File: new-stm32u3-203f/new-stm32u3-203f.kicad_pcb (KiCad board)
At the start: 4 copper layers, 14.5 x 90 mm, 81 parts, among them J1 Display, J2 SJ-3524-SMT, J3 12401826E412A, J4 Battery connector, J5 473092651, J6 UART, J7 RESET, SW1 SW_SPDT, SW3 VOL+, SW4 VOL-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

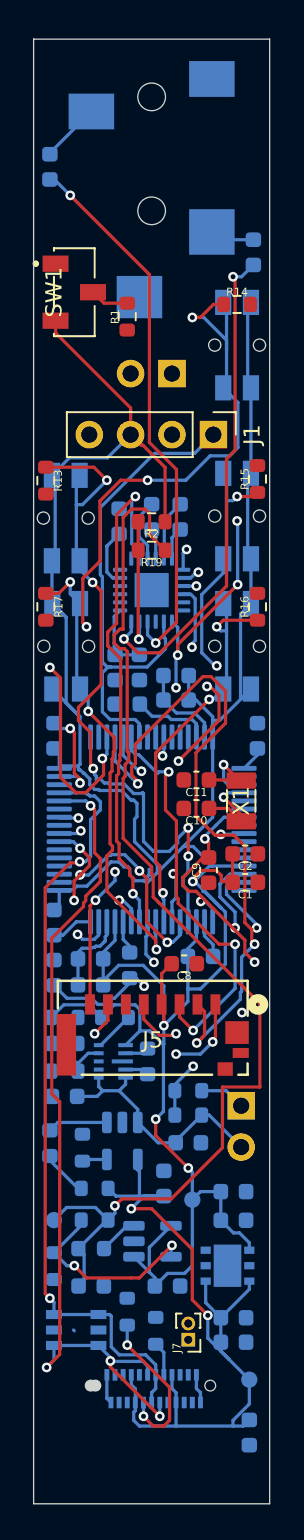
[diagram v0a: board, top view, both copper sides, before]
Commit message: restarted routing and started using 6 layers and power planes.
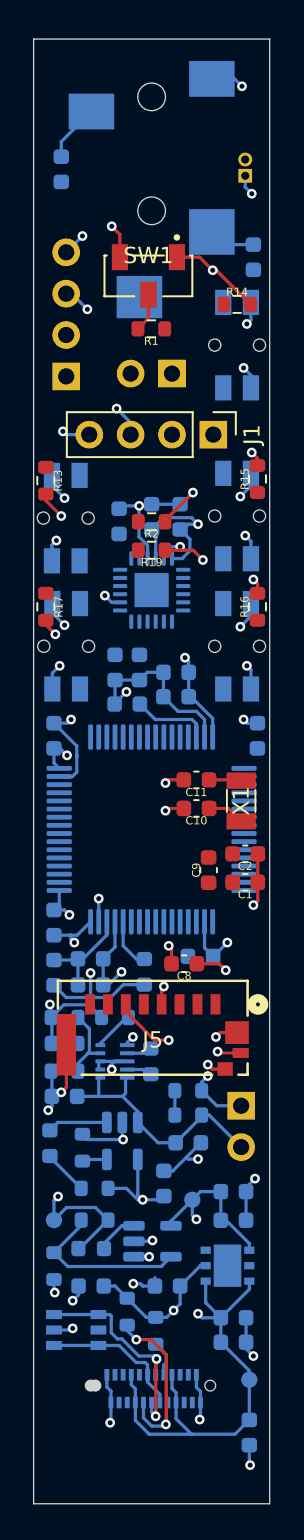
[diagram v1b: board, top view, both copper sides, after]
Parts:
- added J8: SWD, Connector_PinHeader_2.54mm:PinHeader_1x04_P2.54mm_Vertical, B.Cu at (149.0, 81.1)
- J7: moved to B.Cu
- moved J7 71.6 mm to (160.0, 68.8), turned to 0 degrees
- moved SW1 4.66 mm to (154.1, 75.0), turned to 180 degrees
- moved R1 1.66 mm to (154.2, 78.2), turned to 180 degrees
- moved L1 0.98 mm to (153.8, 117.7)
- moved C12 0.72 mm to (148.7, 68.4), turned to 90 degrees
- moved C13 0.30 mm to (160.5, 73.8), turned to 90 degrees
- moved C21 0.20 mm to (155.8, 100.8)
- moved C23 0.20 mm to (155.8, 99.3)
- moved L3 0.20 mm to (154.2, 123.2)
- moved U7 0.10 mm to (152.0, 123.2)
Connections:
- C1 pad 1: GNDA -> USB_GND
- C10 pad 2: GNDA -> USB_GND
- C11 pad 2: GNDA -> USB_GND
- C14 pad 2: GNDA -> USB_GND
- C15 pad 1: GNDA -> USB_GND
- C16 pad 1: GNDA -> USB_GND
- C17 pad 1: GNDA -> USB_GND
- C18 pad 1: GNDA -> USB_GND
- C19 pad 2: GNDA -> USB_GND
- C2 pad 1: GNDA -> USB_GND
- C21 pad 1: GNDA -> USB_GND
- C22 pad 1: GNDA -> USB_GND
- C23 pad 1: GNDA -> USB_GND
- C24 pad 1: GNDA -> USB_GND
- C25 pad 1: GNDA -> USB_GND
- C26 pad 1: GNDA -> USB_GND
- C27 pad 1: GNDA -> USB_GND
- C28 pad 1: GNDA -> USB_GND
- C29 pad 1: GNDA -> USB_GND
- C3 pad 2: GNDA -> USB_GND
- C30 pad 1: GNDA -> USB_GND
- C31 pad 1: GNDA -> USB_GND
- C33 pad 1: GNDA -> USB_GND
- C34 pad 1: GNDA -> USB_GND
- C35 pad 1: GNDA -> USB_GND
- C36 pad 1: GNDA -> USB_GND
- C4 pad 2: GNDA -> USB_GND
- C5 pad 1: GNDA -> USB_GND
- C6 pad 1: GNDA -> USB_GND
- C7 pad 1: GNDA -> USB_GND
- C8 pad 1: GNDA -> USB_GND
- C9 pad 1: GNDA -> USB_GND
- CR1 pad 2: GNDA -> USB_GND
- J1 pad 4: GNDA -> USB_GND
- J2 pad R: (no net) -> HP_RIGHT
- J2 pad S: (no net) -> USB_GND
- J2 pad T: (no net) -> HP_LEFT
- J4 pad 1: GNDA -> USB_GND
- J5 pad 6: GNDA -> USB_GND
- J5 pad G1: GNDA -> USB_GND
- J5 pad G2: GNDA -> USB_GND
- J5 pad G3: GNDA -> USB_GND
- J5 pad G4: GNDA -> USB_GND
- J7 pad 1: GNDA -> USB_GND
- R10 pad 2: GNDA -> USB_GND
- R13 pad 2: GNDA -> USB_GND
- R14 pad 2: GNDA -> USB_GND
- R15 pad 2: GNDA -> USB_GND
- R16 pad 2: GNDA -> USB_GND
- R17 pad 2: GNDA -> USB_GND
- R18 pad 2: GNDA -> USB_GND
- R4 pad 1: GNDA -> USB_GND
- R5 pad 2: GNDA -> USB_GND
- R7 pad 2: GNDA -> USB_GND
- R9 pad 1: GNDA -> USB_GND
- SW1 pad 1: GNDA -> USB_GND
- U1 pad 12: GNDA -> USB_GND
- U1 pad 18: GNDA -> USB_GND
- U1 pad 30: GNDA -> USB_GND
- U1 pad 32: GNDA -> USB_GND
- U1 pad 46: unconnected-(U1A-PA13-Pad46) -> SWDCLK
- U1 pad 47: GNDA -> USB_GND
- U1 pad 49: unconnected-(U1A-PA14-Pad49) -> SWDDIO
- U1 pad 63: GNDA -> USB_GND
- U2 pad 14: GNDA -> USB_GND
- U2 pad 21: GNDA -> USB_GND
- U2 pad 23: GNDA -> USB_GND
- U4 pad 2: GNDA -> USB_GND
- U4 pad 7: GNDA -> USB_GND
- U5 pad 2: GNDA -> USB_GND
- U6 pad 2: GNDA -> USB_GND
- U7 pad 2: GNDA -> USB_GND
- U7 pad 3: GNDA -> USB_GND
- U7 pad 8: GNDA -> USB_GND
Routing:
- net AVDD: track 197.0 -> 62.0 mm, vias 4 -> 25
- net USB_GND: track 3.61 -> 121.5 mm, vias 0 -> 42
- net sk_btn_2: track 61.2 -> 0.00 mm, vias 6 -> 0
- net UART_TX: track 53.2 -> 0.00 mm, vias 1 -> 0
- net +1V8: track 72.2 -> 21.0 mm, vias 1 -> 4
- net SD_DAT2: track 47.6 -> 0.00 mm, vias 4 -> 0
- net UART_RX: track 45.5 -> 0.00 mm, vias 1 -> 0
- net USB_D-: track 52.5 -> 8.87 mm, vias 4 -> 0
- net ps_btn_1: track 43.1 -> 0.00 mm, vias 5 -> 0
- net SD_DAT3: track 42.5 -> 0.00 mm, vias 3 -> 0
- net /MCU_IO/NRST: track 37.5 -> 0.00 mm, vias 3 -> 0
- net UBS_D+: track 47.4 -> 13.7 mm
- net v+_btn_3: track 33.1 -> 0.00 mm, vias 5 -> 0
- net DAC_RST: track 32.0 -> 0.00 mm, vias 2 -> 0
- net GNDA: track 31.9 -> 0.00 mm, vias 2 -> 0
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- added copper zone on In2.Cu, net +1V8
- added copper zone on In3.Cu, net AVDD
- added copper zone on In1.Cu, net USB_GND
- added copper zone on In4.Cu, net USB_GND
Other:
- copper layers 4 -> 6

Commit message: finished routing, need angus to check
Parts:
- moved J7 76.5 mm to (148.2, 144.4)
- moved C11 6.14 mm to (160.4, 100.8), turned to 90 degrees
- moved C10 3.33 mm to (160.3, 108.1), turned to -90 degrees
- moved X1 2.64 mm to (160.2, 104.6)
- moved C22 2.03 mm to (159.2, 116.2), turned to -90 degrees
- moved C9 0.65 mm to (157.1, 111.5)
- turned C12 to -90 degrees
- turned C13 to -90 degrees
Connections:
- J2 pad R: HP_RIGHT -> Net-(J2-R)
- J2 pad T: HP_LEFT -> Net-(J2-L)
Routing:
- net sk_btn_2: track 0.00 -> 56.3 mm, vias 0 -> 5
- net +1V8: track 21.0 -> 77.3 mm, vias 4 -> 3
- net v+_btn_3: track 0.00 -> 55.9 mm, vias 0 -> 3
- net ps_btn_1: track 0.00 -> 50.8 mm, vias 0 -> 3
- net /MCU_IO/NRST: track 0.00 -> 47.1 mm, vias 0 -> 1
- net UART_TX: track 0.00 -> 40.0 mm, vias 0 -> 1
- net pp_btn_5: track 0.00 -> 39.4 mm, vias 0 -> 4
- net UART_RX: track 0.00 -> 38.5 mm, vias 0 -> 1
- net USB_D-: track 8.87 -> 47.0 mm, vias 0 -> 2
- net UBS_D+: track 13.7 -> 49.1 mm, vias 2 -> 4
- net HP_RIGHT: track 3.54 -> 38.2 mm, vias 0 -> 2
- net I2C_SDA: track 0.00 -> 34.1 mm, vias 0 -> 2
- net DAC_RST: track 0.00 -> 31.4 mm, vias 0 -> 2
- net I2C1_SCL: track 0.00 -> 30.4 mm
- net HP_LEFT: track 2.87 -> 33.1 mm, vias 0 -> 2
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- added copper zone on B.Cu, net USB_GND
- added copper zone on F.Cu, net USB_GND
- added copper zone on In2.Cu, net USB_GND
- removed copper zone on In2.Cu, net +1V8

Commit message: ficxed all the vias and some routing, will need to add in ground stitching
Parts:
- moved C11 1.41 mm to (159.4, 101.8), turned to 0 degrees
- moved R2 0.95 mm to (154.2, 89.1)
- moved C25 0.45 mm to (160.3, 103.2)
- moved C18 0.30 mm to (156.3, 89.8)
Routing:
- net AVDD: track 74.7 -> 93.1 mm, vias 28 -> 25
- net USB_GND: track 132.8 -> 135.9 mm, vias 53 -> 49
- net +1V8: track 77.3 -> 74.7 mm
- net OSC_IN: track 6.98 -> 9.37 mm
- net OSC_OUT: track 5.48 -> 6.76 mm
- net Net-(U2-LDOIN/HPVDD): track 8.20 -> 9.17 mm
- net SCK_A: track 27.8 -> 28.6 mm
- net SWDCLK: track 27.8 -> 28.4 mm

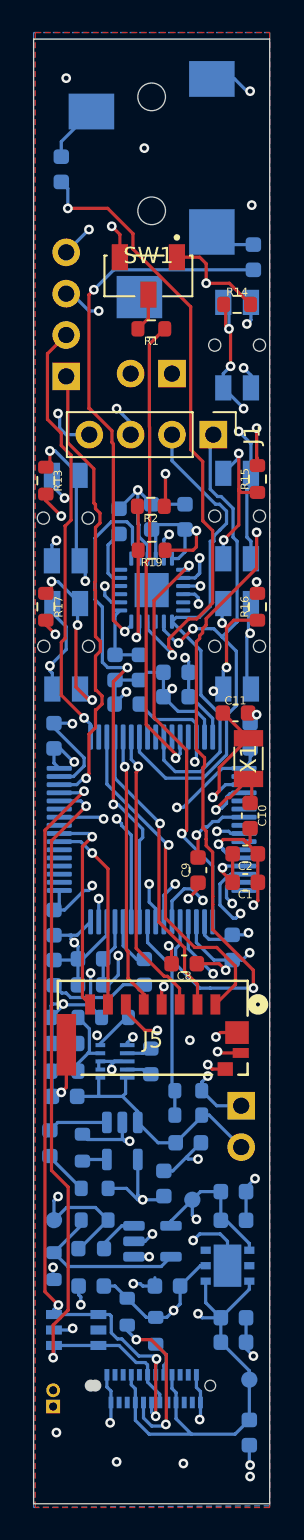
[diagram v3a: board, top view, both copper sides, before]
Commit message: added usb sheilding and more stiching vias
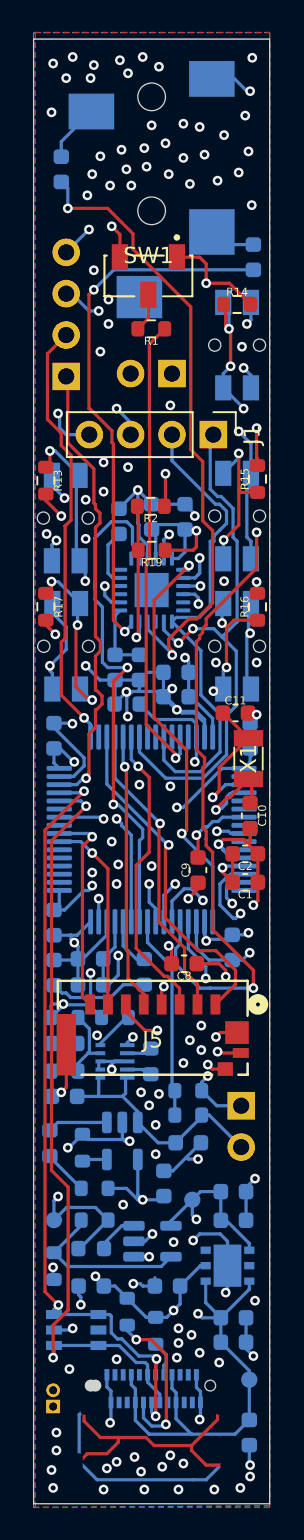
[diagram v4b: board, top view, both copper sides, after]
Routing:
- net USB_GND: track 135.9 -> 228.8 mm, vias 49 -> 141
- net SD_CMD: track 17.9 -> 18.5 mm
- net /MCU_IO/NRST: track 47.1 -> 46.8 mm, vias 1 -> 2

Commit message: fixed silkscreen.
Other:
- board text added: "Made By: Isaac Norris"
- board text added: "P3-U3 V1.0"

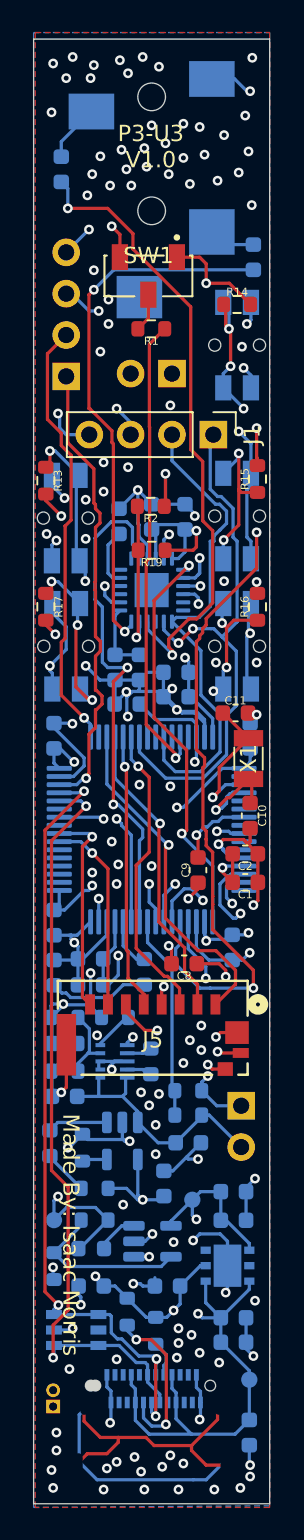
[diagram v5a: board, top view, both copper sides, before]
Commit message: fixed some of the drc erros will need to complete more.
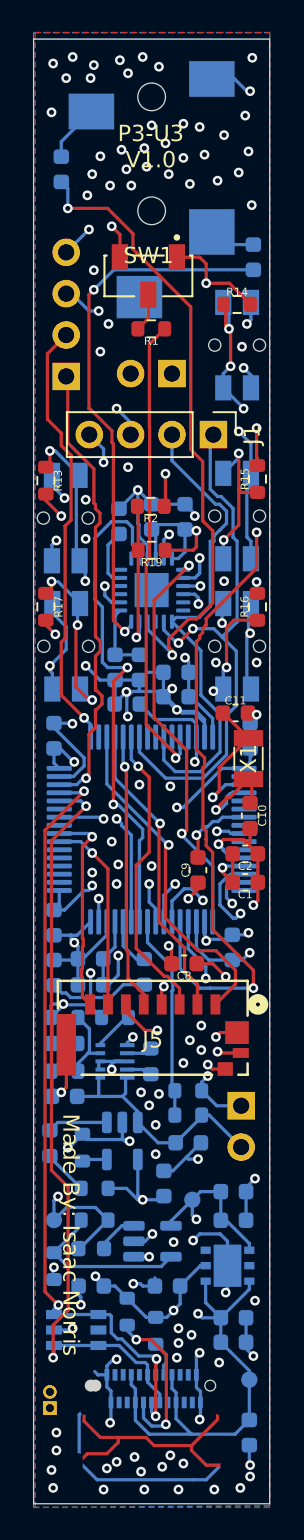
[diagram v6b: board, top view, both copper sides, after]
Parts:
- moved J7 0.22 mm to (148.0, 144.5)
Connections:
- J2 pad R: Net-(J2-R) -> (no net)
- J2 pad S: USB_GND -> (no net)
- J2 pad T: Net-(J2-L) -> (no net)
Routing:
- net USB_GND: track 228.8 -> 231.3 mm, vias 141 -> 134
- net /MCU_IO/NRST: vias 2 -> 1

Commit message: finished more errors, started adding extra stuff.
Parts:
- moved C1 0.50 mm to (159.5, 112.2)
- moved C2 0.50 mm to (159.5, 110.5)
- moved R15 0.48 mm to (160.3, 87.6)
- moved X1 0.40 mm to (159.8, 104.6)
- moved R13 0.27 mm to (147.9, 87.3)
- moved R17 0.25 mm to (148.0, 95.3)
- moved R16 0.25 mm to (160.5, 95.3)
- moved J8 0.10 mm to (149.1, 81.1)
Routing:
- net AVDD: track 93.3 -> 90.1 mm
- net USB_GND: track 231.3 -> 233.6 mm, vias 134 -> 135
- net MCLK_A: track 25.0 -> 26.1 mm

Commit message: fixed drc and some other things.
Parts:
- moved R13 0.30 mm to (148.2, 87.3)
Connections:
- J2 pad R: (no net) -> Net-(J2-R)
- J2 pad S: (no net) -> USB_GND
- J2 pad T: (no net) -> Net-(J2-L)
- J3 pad : (no net) -> USB_GND
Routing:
- net USB_GND: track 233.6 -> 158.0 mm, vias 135 -> 136
- net I2C1_SCL: track 30.3 -> 29.2 mm
